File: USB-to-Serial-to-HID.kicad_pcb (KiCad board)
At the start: 2 copper layers, 37.7 x 17.5 mm, 11 parts, among them J2 USB4520-03-1-A, J3 48037-2200, U1 CH340E, U2 CH9329

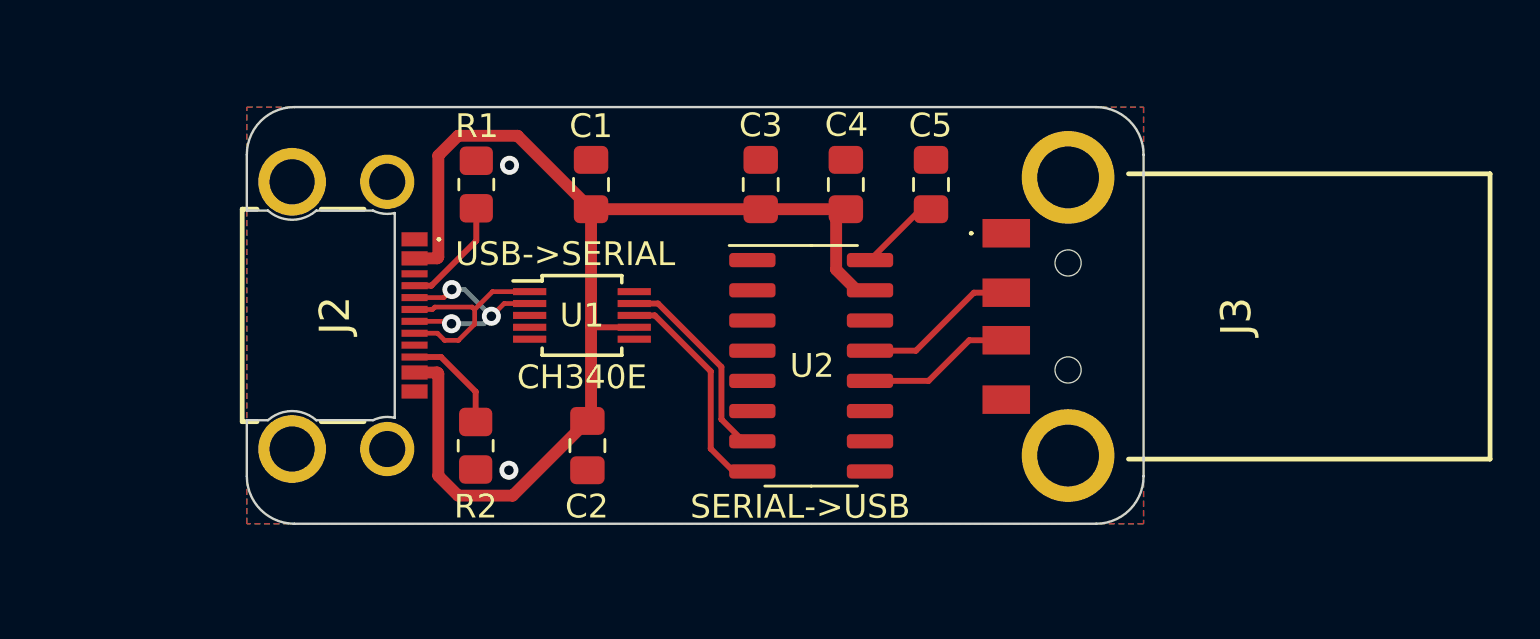
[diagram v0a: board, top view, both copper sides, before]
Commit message: Move to CH340C
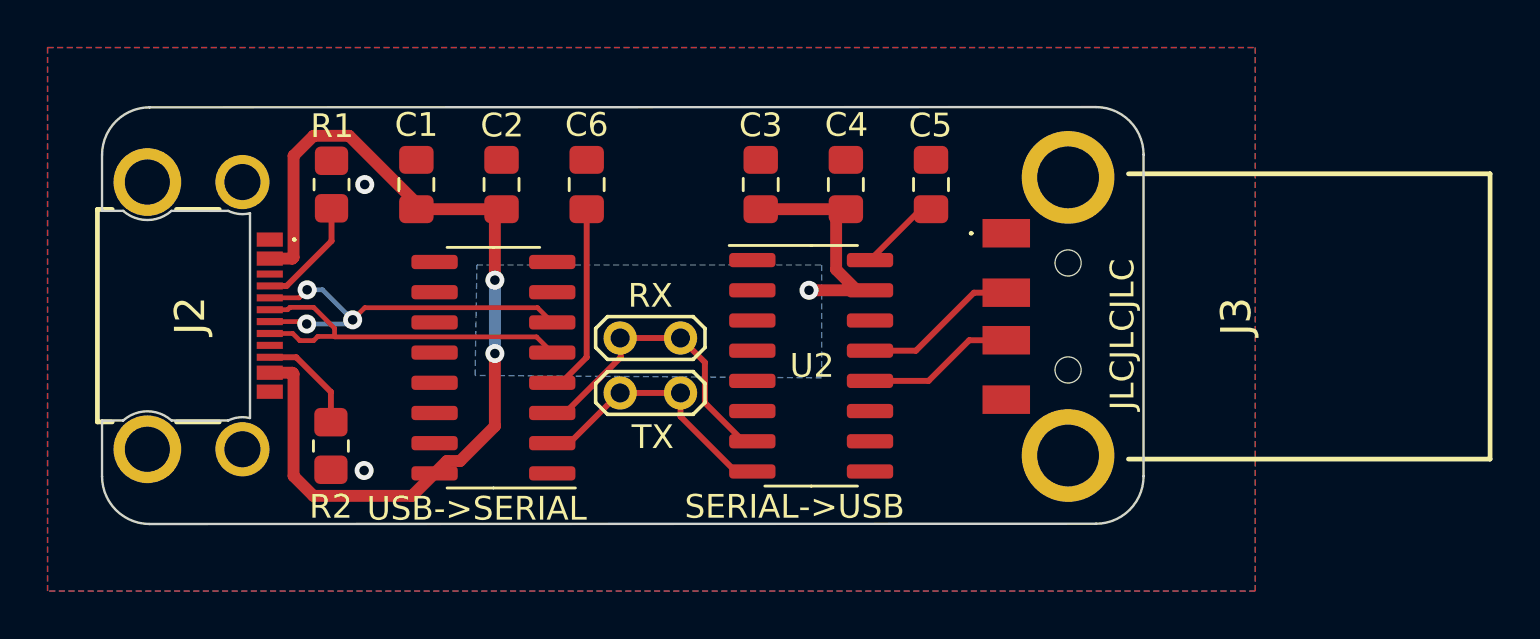
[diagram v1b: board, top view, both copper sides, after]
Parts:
- added C6: 100nF, Capacitor_SMD:C_0805_2012Metric_Pad1.18x1.45mm_HandSolder, F.Cu at (124.3, 69.3)
- added JP1: TX, TestPoint:TestPoint_2Pads_Pitch2.54mm_Drill0.8mm, F.Cu at (128.2, 78.0)
- added JP2: RX, TestPoint:TestPoint_2Pads_Pitch2.54mm_Drill0.8mm, F.Cu at (128.2, 75.7)
- U1: value CH340E -> CH340C; footprint Package_SO:MSOP-10_3x3mm_P0.5mm -> Package_SO:SOIC-16_3.9x9.9mm_P1.27mm
- moved C2 11.6 mm to (120.7, 69.3), turned to 90 degrees
- moved C1 7.35 mm to (117.1, 69.3)
- moved J2 6.09 mm to (106.9, 74.8)
- moved R2 6.09 mm to (113.5, 80.3)
- moved R1 6.09 mm to (113.5, 69.3)
- moved U1 4.33 mm to (120.4, 77.0), turned to 180 degrees
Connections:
- U1 pad 1: DI+ -> GND
- U1 pad 2: DI- -> CH340_TX
- U1 pad 3: GND -> CH340_RX
- U1 pad 4: unconnected-(U1-~{RTS}-Pad4) -> Net-(U1-V3)
- U1 pad 5: unconnected-(U1-~{CTS}-Pad5) -> DI+
- U1 pad 6: unconnected-(U1-TNOW-Pad6) -> DI-
- U1 pad 7: USB_VIN -> unconnected-(U1-NC-Pad7)
- U1 pad 8: CH340E_TX -> unconnected-(U1-NC-Pad8)
- U1 pad 9: CH340E_RX -> unconnected-(U1-~{CTS}-Pad9)
- U2 pad 7: CH340E_RX -> CH340_RX
- U2 pad 8: CH340E_TX -> CH340_TX
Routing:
- net CH340_RX: track 0.00 -> 13.1 mm
- net CH340_TX: track 0.00 -> 11.3 mm
- net CH340E_TX: track 9.59 -> 0.00 mm
- net CH340E_RX: track 8.66 -> 0.00 mm
- net Net-(U1-V3): track 0.00 -> 8.04 mm
- net DI-: track 9.07 -> 16.6 mm
- net DI+: track 8.79 -> 15.8 mm
- net USB_VIN: track 53.1 -> 51.3 mm, vias 0 -> 3
- added copper zone on B.Cu, net USB_VIN
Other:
- board size 37.7 x 17.5 mm -> 43.8 x 17.5 mm
- board text added: "JLCJLCJLC"
